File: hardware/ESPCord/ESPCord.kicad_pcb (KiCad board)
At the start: 2 copper layers, 17.4 x 29.9 mm, 8 parts, among them J1 USB_C_Receptacle, K1 SRD-03VDC-SL-C, U1 ESP32-C3, U2 AMS1117-3_3_C347222

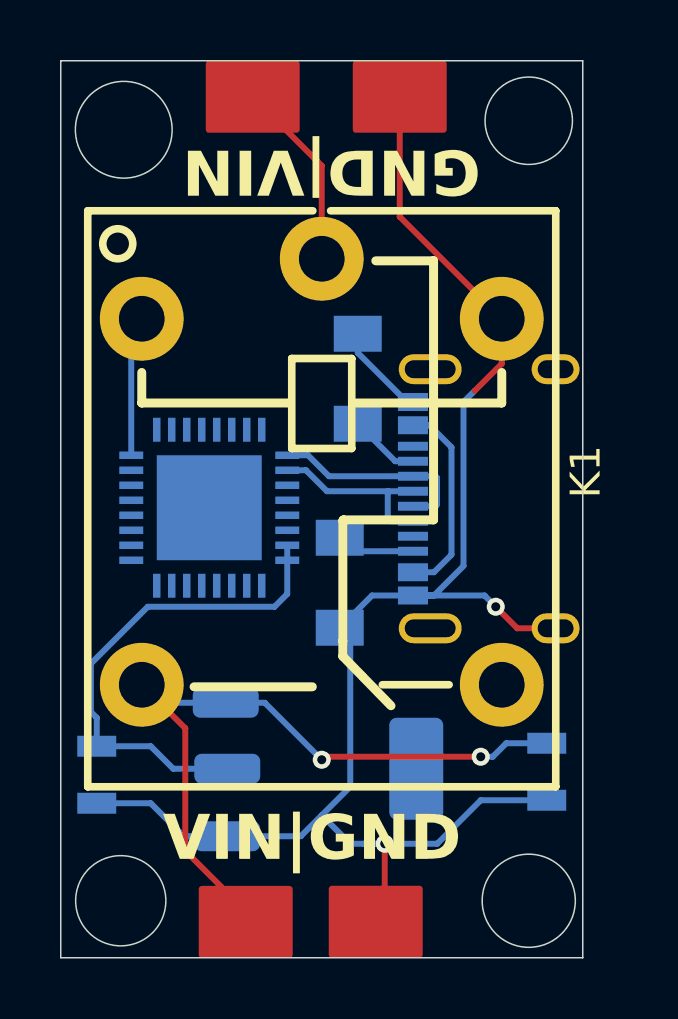
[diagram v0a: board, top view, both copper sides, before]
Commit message: final touches, thickened the routes and altered zine
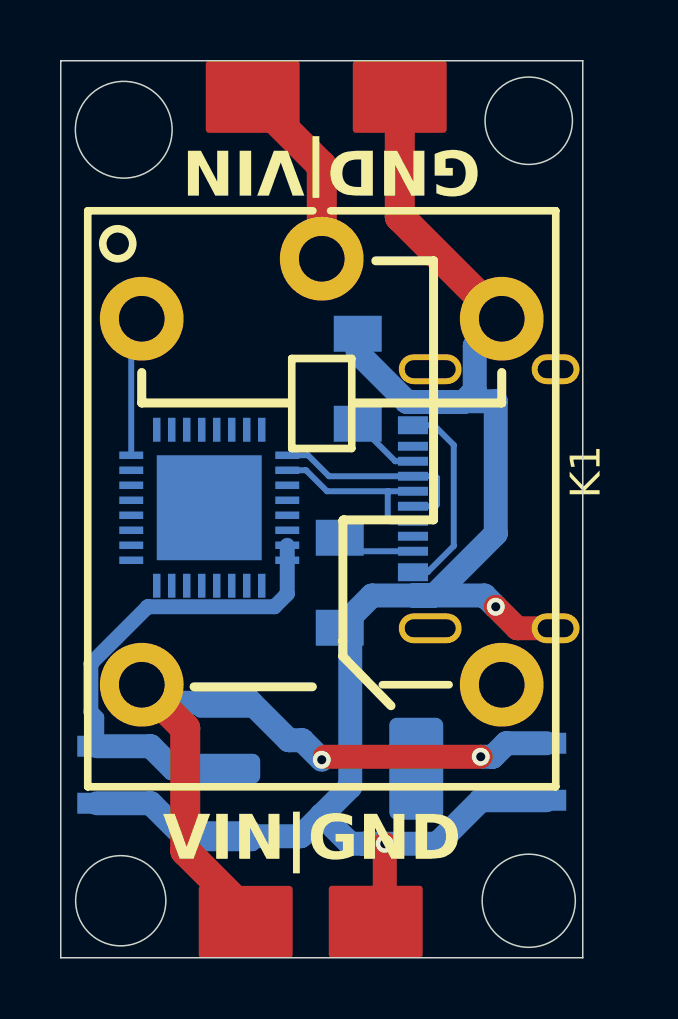
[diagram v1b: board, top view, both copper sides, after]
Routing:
- net GND: track 59.6 -> 61.1 mm
